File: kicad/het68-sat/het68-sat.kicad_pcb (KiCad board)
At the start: 6 copper layers, 50 x 80 mm, 40 parts, among them J1 RJ45, U1 AP2112K-1.8, U2 SN65LVDS2, U3 SN65LVDS2, U4 SN65LVDS1, U5 TXS0104E

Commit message: Ship v4.1.0 as a Core+satellite+power kit without the v3 HAT.
LVDS now has 100 ohm receivers, SD common-mode chokes, and 3V3 ferrites for a noisy line; the kit BOM and 3D previews match that schematic.

Co-authored-by: Cursor <cursoragent@cursor.com>
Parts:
- added FB1: 600R, Inductor_SMD:L_0603_1608Metric, F.Cu at (40.0, 18.0)
- added R_SCK: 100, Resistor_SMD:R_0603_1608Metric, F.Cu at (13.0, 38.0)
- added R_WS: 100, Resistor_SMD:R_0603_1608Metric, F.Cu at (23.0, 38.0)
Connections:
- F1 pad 2: +3V3 -> +3V3_FB
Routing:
- net GND: vias 124 -> 164

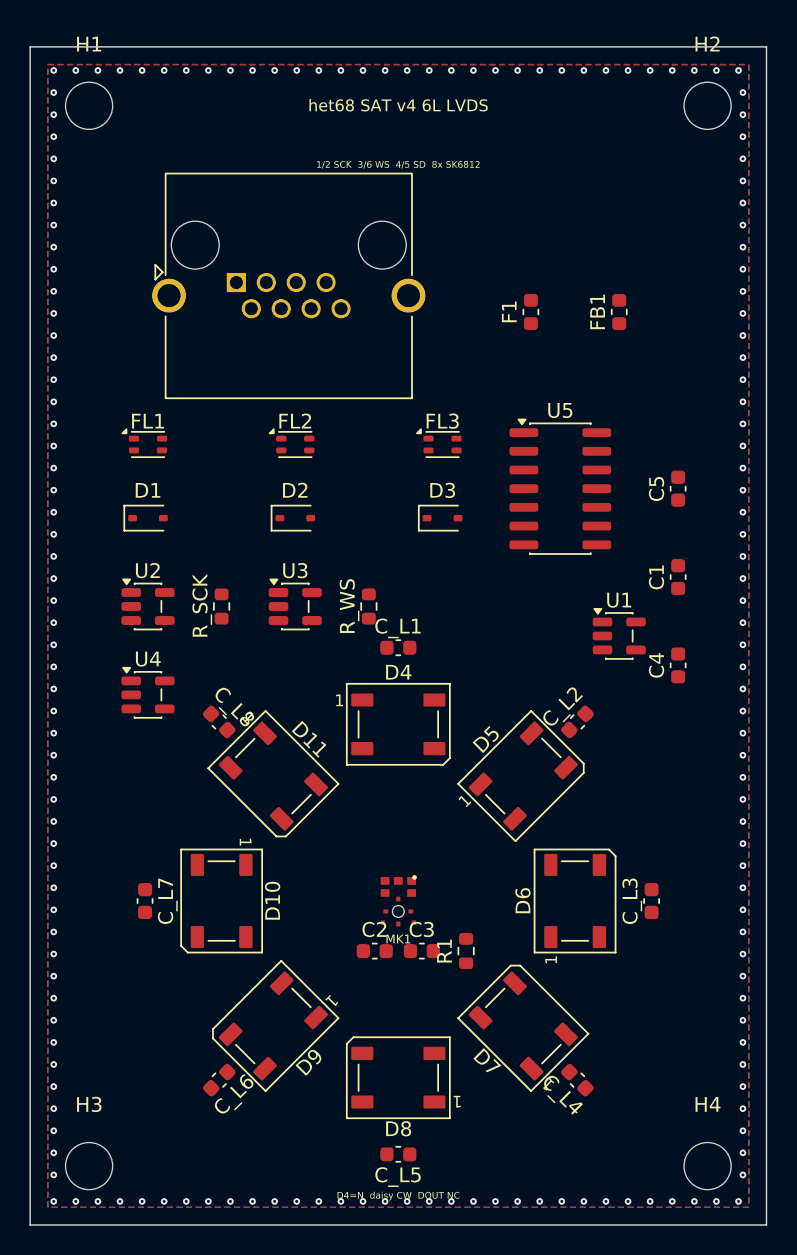
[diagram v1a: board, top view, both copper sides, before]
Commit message: Add a Core status LED and three buttons, and fit a 21700 holder.
RESET, BOOT and USER sit on the east edge with one SK6812; the power board uses a Keystone 1122 instead of an 18650 sled. Masks, schematics and JLCPCB gerber zips are in the tree.

Co-authored-by: Cursor <cursoragent@cursor.com>
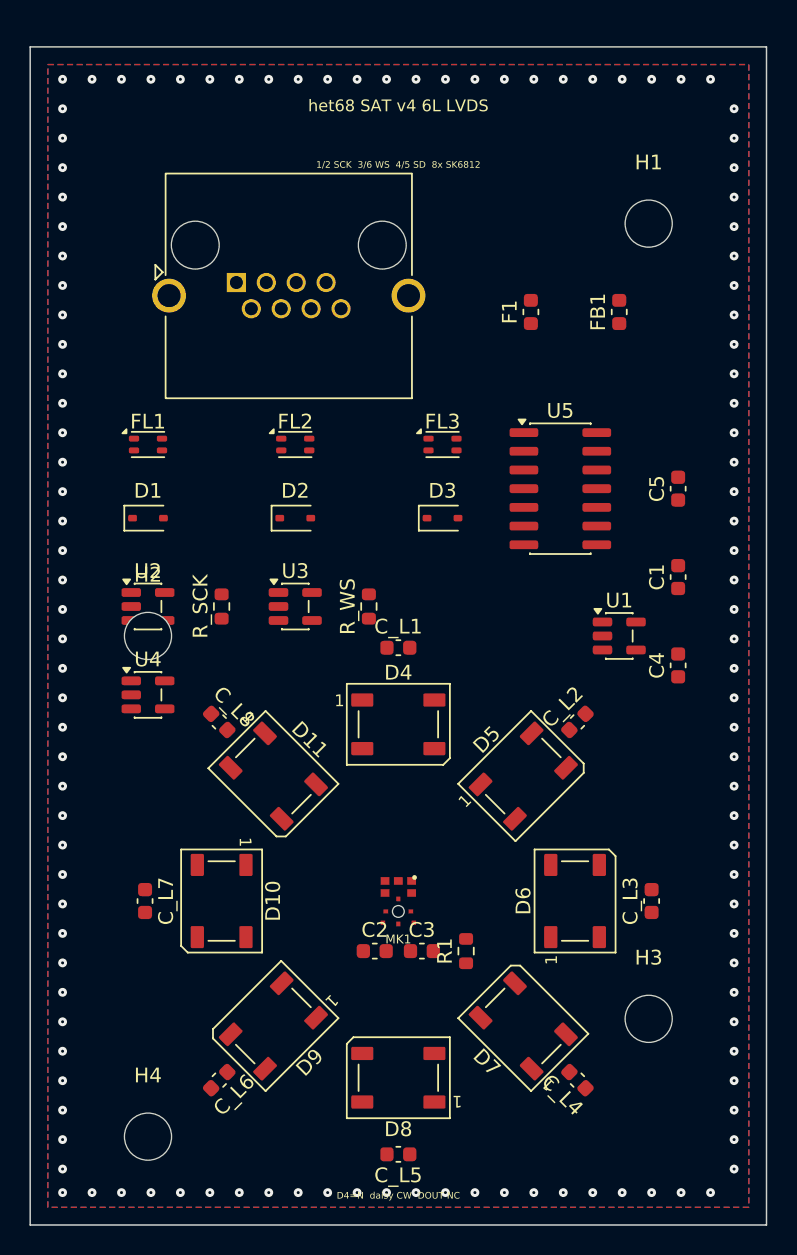
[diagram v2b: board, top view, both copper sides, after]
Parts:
- moved H2 52.3 mm to (8.00, 40.0)
- moved H3 39.3 mm to (42.0, 66.0)
- moved H1 38.8 mm to (42.0, 12.0)
- moved H4 38.1 mm to (8.00, 74.0)
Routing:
- net GND: vias 164 -> 120

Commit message: Route signal copper on the five v4 boards and drop tracks that still short.
Core and the satellite have no copper shorts left. QFN-80 fanout and a few LVDS pairs stay open, and the power boards still have overlapping pads from placement.

Co-authored-by: Cursor <cursoragent@cursor.com>
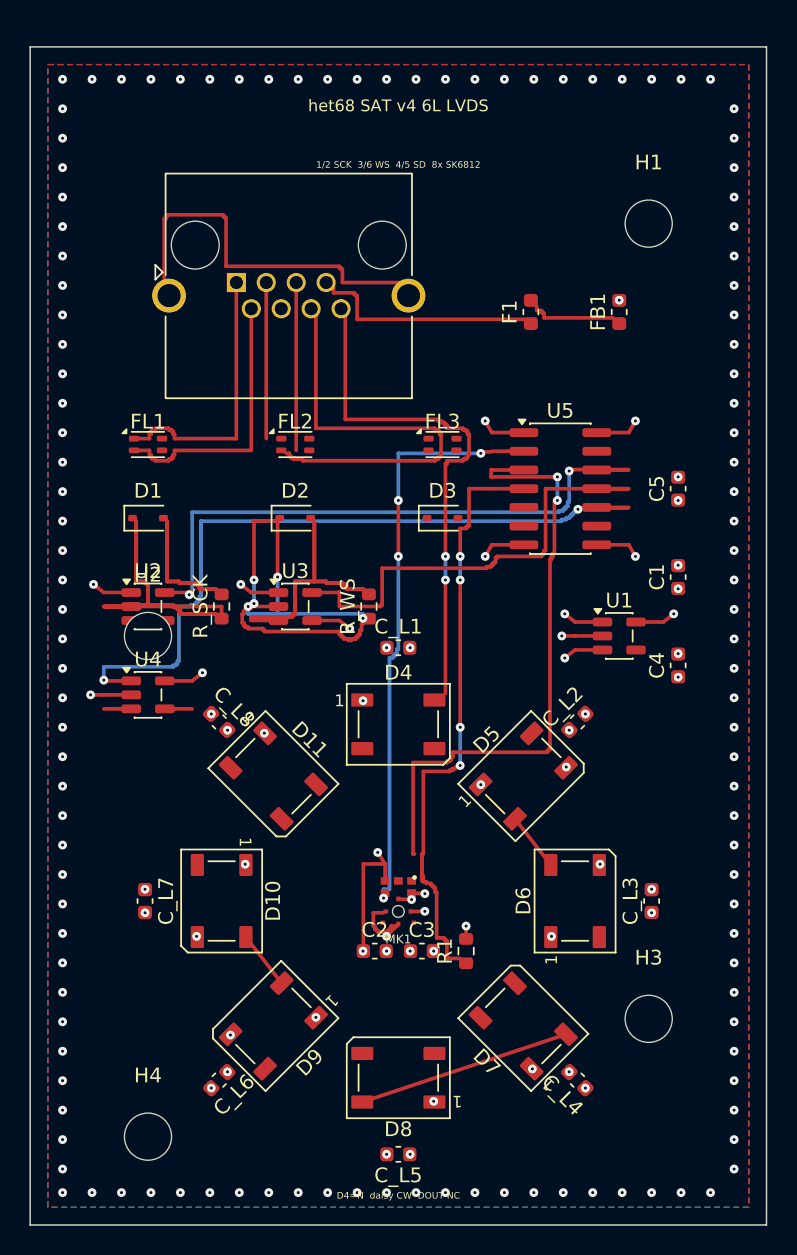
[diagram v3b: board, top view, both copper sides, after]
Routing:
- net SD_3V3: track 0.00 -> 51.3 mm, vias 0 -> 2
- net SD: track 0.00 -> 43.5 mm, vias 0 -> 4
- net SCK_3V3: track 0.00 -> 42.7 mm, vias 0 -> 2
- net WS: track 0.00 -> 42.7 mm, vias 0 -> 2
- net SCK: track 0.00 -> 40.2 mm, vias 0 -> 4
- net SCK_P: track 0.00 -> 39.4 mm
- net WS_P: track 0.00 -> 37.6 mm, vias 0 -> 5
- net LED: track 0.00 -> 36.7 mm, vias 0 -> 2
- net WS_3V3: track 0.00 -> 32.6 mm
- net WS_N: track 0.00 -> 32.4 mm
- net WS_NJ: track 0.00 -> 30.0 mm
- net unconnected-(J1-SHIELD-PadSH): track 0.00 -> 27.0 mm
- net GND: track 0.00 -> 20.2 mm, vias 120 -> 146
- net +3V3: track 0.00 -> 19.9 mm, vias 0 -> 27
- net SCK_NJ: track 0.00 -> 19.0 mm
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
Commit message: Fan out the RP2350B and finish the signal bridges that can leave the package.
Each QFN pin gets a 0.15 mm escape along its axis. The crystal moves off the north row so that corridor exists. Core and the satellite have no new shorts; a few center-row pins and some LVDS nets are still open.

Co-authored-by: Cursor <cursoragent@cursor.com>
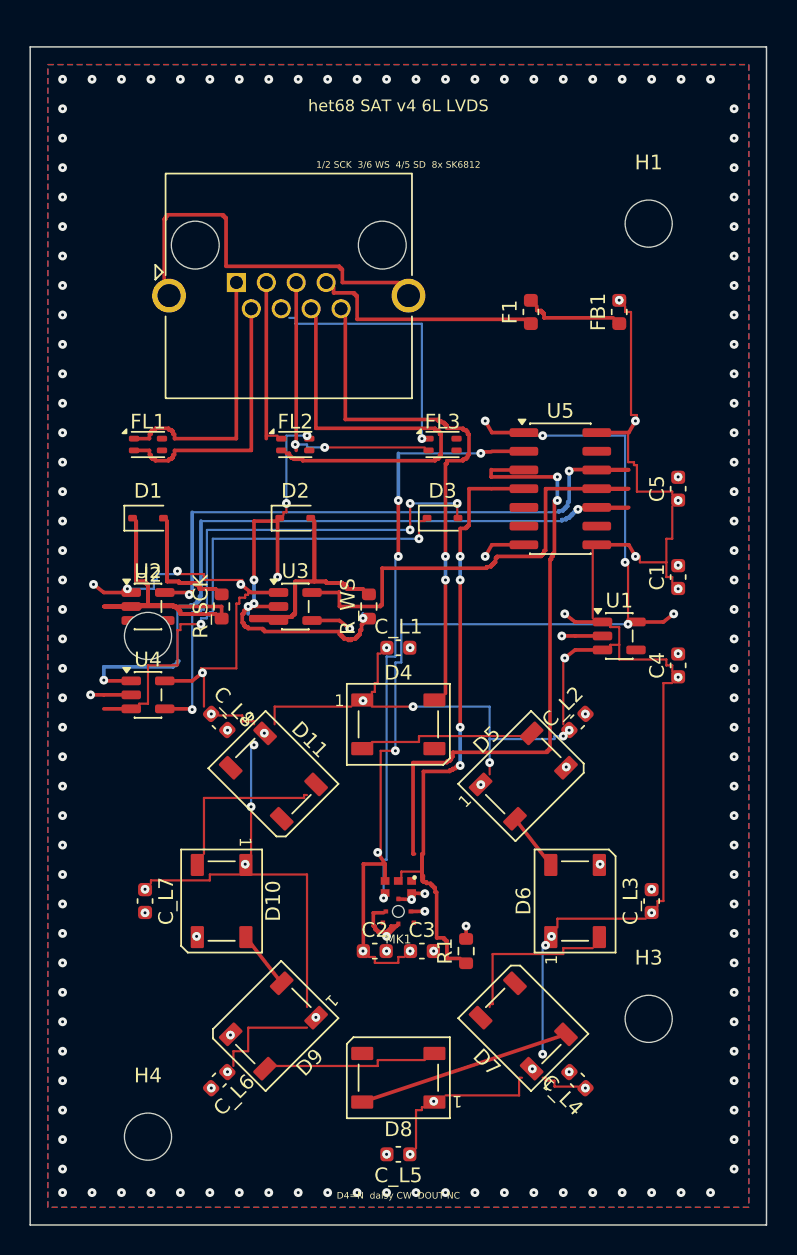
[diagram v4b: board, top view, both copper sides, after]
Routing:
- net +3V3: track 19.9 -> 190.9 mm, vias 27 -> 36
- net +1V8: track 15.3 -> 69.5 mm, vias 5 -> 9
- net SD_N: track 2.25 -> 35.1 mm, vias 0 -> 4
- net SD_P: track 2.25 -> 34.3 mm, vias 0 -> 2
- net SD_PJ: track 0.00 -> 17.4 mm, vias 0 -> 1
- net LED4: track 0.00 -> 11.0 mm
- net LED8: track 0.00 -> 11.0 mm
- net LED6: track 0.00 -> 10.6 mm
- net LED2: track 0.00 -> 10.6 mm
- net SD_NJ: track 11.4 -> 20.4 mm, vias 0 -> 2
- net WS_P: track 37.6 -> 34.3 mm, vias 5 -> 7
- net SD: track 43.5 -> 45.3 mm
- net WS_PJ: track 10.6 -> 11.4 mm

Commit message: Put the satellite electronics on the back and clear the power-board pad shorts.
The outward face keeps only the microphone hole and the eight SK6812s. The DO-201 and the two regulators move off the header so the power boards no longer short pad to pad. Some LVDS, QSPI and GPIO nets are still open.

Co-authored-by: Cursor <cursoragent@cursor.com>
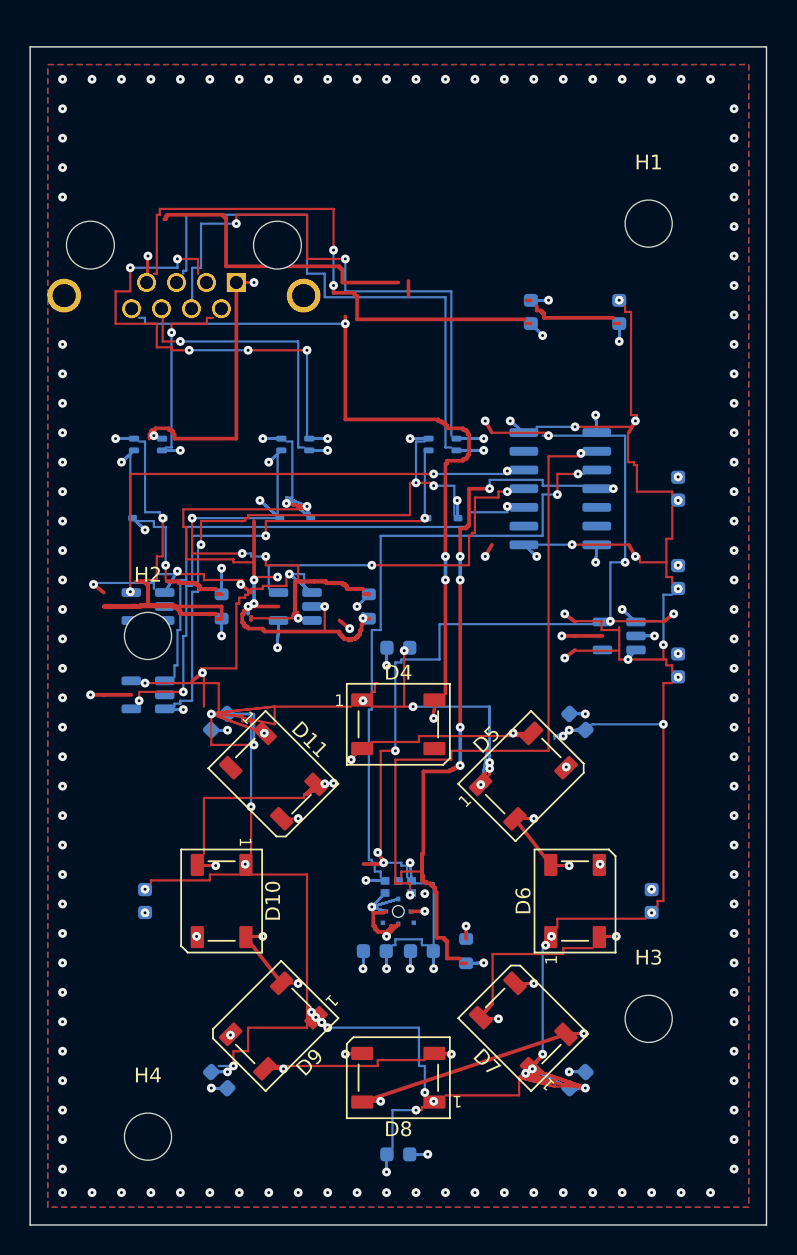
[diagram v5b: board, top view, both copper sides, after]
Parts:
- C1, C2, C3, C4, C5, C_L1, C_L2, C_L3, C_L4, C_L5, C_L6, C_L7, C_L8, D1, D2, D3, F1, FB1, FL1, FL2, FL3, J1, MK1, R1, R_SCK, R_WS, U1, U2, U3, U4, U5: moved to B.Cu
- turned C2 to 180 degrees
- turned C3 to 180 degrees
- turned C_L1 to 180 degrees
- turned C_L2 to 135 degrees
- turned C_L4 to 45 degrees
- turned C_L5 to 0 degrees
- turned C_L6 to -45 degrees
- turned C_L8 to -135 degrees
- turned D1 to 180 degrees
- turned D2 to 180 degrees
- turned D3 to 180 degrees
- turned FL1 to 180 degrees
- turned FL2 to 180 degrees
- turned FL3 to 180 degrees
- turned J1 to 180 degrees
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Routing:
- net +3V3: track 190.9 -> 510.8 mm, vias 36 -> 54
- net GND: track 20.2 -> 187.8 mm, vias 146 -> 148
- net WS_P: track 34.3 -> 94.8 mm, vias 7 -> 9
- net LED8: track 11.0 -> 56.4 mm, vias 0 -> 3
- net 3V3_F: track 16.0 -> 61.1 mm, vias 0 -> 4
- net WS_N: track 32.4 -> 74.4 mm, vias 0 -> 7
- net SD_PJ: track 17.4 -> 53.2 mm, vias 1 -> 3
- net SD_P: track 34.3 -> 69.5 mm, vias 2 -> 6
- net SCK_N: track 16.7 -> 51.3 mm, vias 0 -> 4
- net +1V8: track 69.5 -> 103.4 mm, vias 9 -> 12
- net SD_NJ: track 20.4 -> 52.8 mm, vias 2 -> 1
- net WS_PJ: track 11.4 -> 41.6 mm, vias 0 -> 6
- net LED4: track 11.0 -> 35.6 mm, vias 0 -> 2
- net LED: track 36.7 -> 60.6 mm, vias 2 -> 4
- net SCK_P: track 39.4 -> 62.1 mm, vias 0 -> 3
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
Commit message: Ship the furthest routed v4 boards with matching previews.
The satellite signal nets are closed, the five boards have no shorts, and the gerbers and renders follow this copper.

Co-authored-by: Cursor <cursoragent@cursor.com>
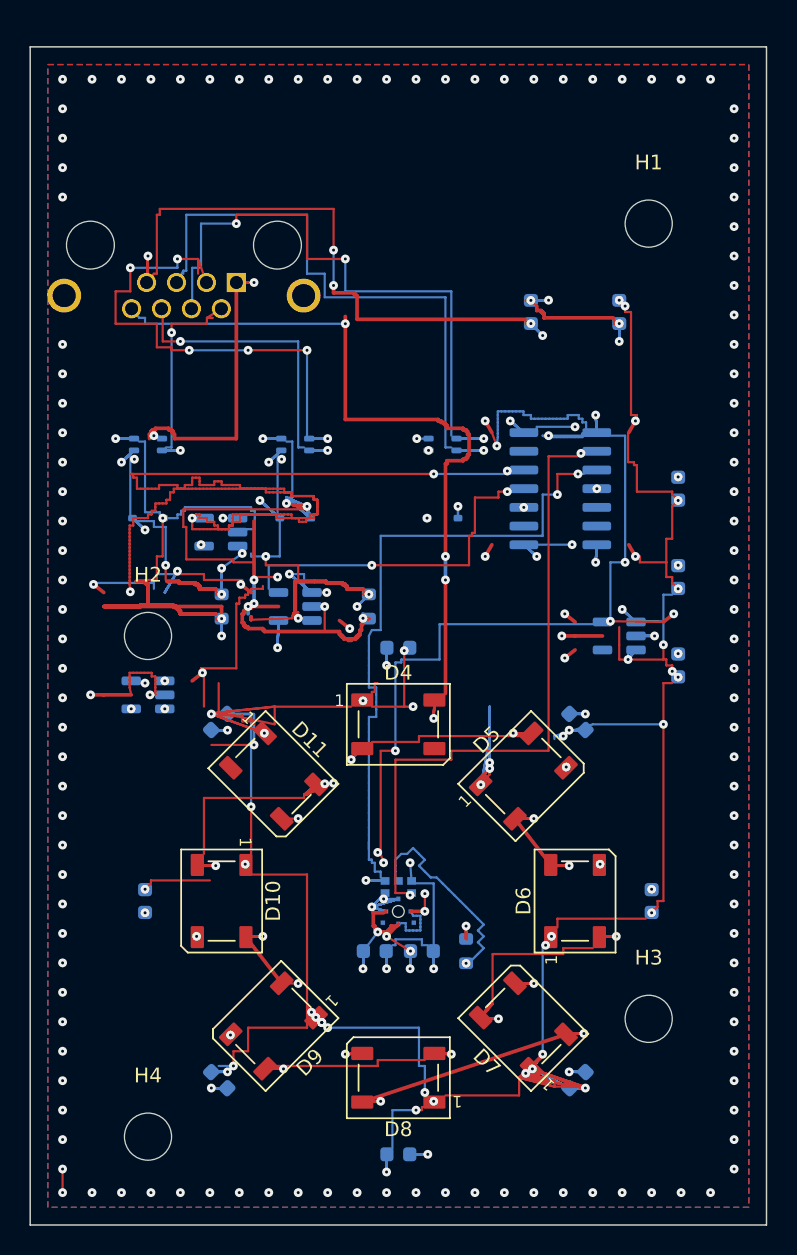
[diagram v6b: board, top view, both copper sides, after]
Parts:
- moved U2 7.07 mm to (12.9, 33.0)
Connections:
- D11 pad 2: unconnected-(D11-DOUT-Pad2) -> (no net)
- J1 pad SH: unconnected-(J1-SHIELD-PadSH) -> (no net)
- MK1 pad 4: unconnected-(MK1-WAKE-Pad4) -> (no net)
- MK1 pad 5: unconnected-(MK1-THSEL-Pad5) -> (no net)
- U1 pad 4: unconnected-(U1-NC-Pad4) -> (no net)
- U5 pad 13: unconnected-(U5-NC2-Pad13) -> (no net)
- U5 pad 5: unconnected-(U5-A4-Pad5) -> (no net)
- U5 pad 6: unconnected-(U5-NC-Pad6) -> (no net)
- U5 pad 9: unconnected-(U5-B4-Pad9) -> (no net)
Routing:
- net SCK_3V3: track 34.9 -> 88.7 mm, vias 3 -> 4
- net +3V3: track 510.8 -> 485.4 mm, vias 54 -> 58
- net unconnected-(J1-SHIELD-PadSH): track 21.8 -> 0.00 mm
- net GND: track 187.8 -> 205.1 mm, vias 148 -> 153
- net SD_P: track 69.5 -> 56.0 mm, vias 6 -> 3
- net SCK_P: track 62.1 -> 71.9 mm, vias 3 -> 4
- net WS_N: track 74.4 -> 66.2 mm
- net SD: track 61.2 -> 68.8 mm, vias 7 -> 2
- net +1V8: track 103.4 -> 108.6 mm, vias 12 -> 13
- net SD_N: track 36.4 -> 38.5 mm, vias 4 -> 3
- net SCK_N: track 51.3 -> 53.4 mm, vias 4 -> 7
- net WS_PJ: track 41.6 -> 43.3 mm
- net WS: track 53.2 -> 54.8 mm
- net SD_3V3: track 35.3 -> 33.9 mm, vias 1 -> 2
- net SCK_NJ: track 22.0 -> 23.2 mm
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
